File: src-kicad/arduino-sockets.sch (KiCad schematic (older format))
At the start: 48 parts, among them J10 1x8_female_pin_Header_2.54mm, J11 1x6_female_pin_Header_2.54mm, J12 1x6_male_pin_Header_2.54mm, J13 1x6_male_pin_Header_2.54mm, J14 1x6_male_pin_Header_2.54mm, J19 2x4_male_pin_Header_2.54mm, J2 1x6_male_pin_Header_2.54mm, J3 1x6_male_pin_Header_2.54mm, J4 1x10_female_pin_Header_2.54mm, J5 1x8_female_pin_Header_2.54mm, J6 1x6_male_pin_Header_2.54mm, J7 1x8_male_pin_Header_2.54mm, J8 1x8_male_pin_Header_2.54mm, J9 1x8_male_pin_Header_2.54mm, U6 TXB0106, U8 TXB0108, U9 TXB0108

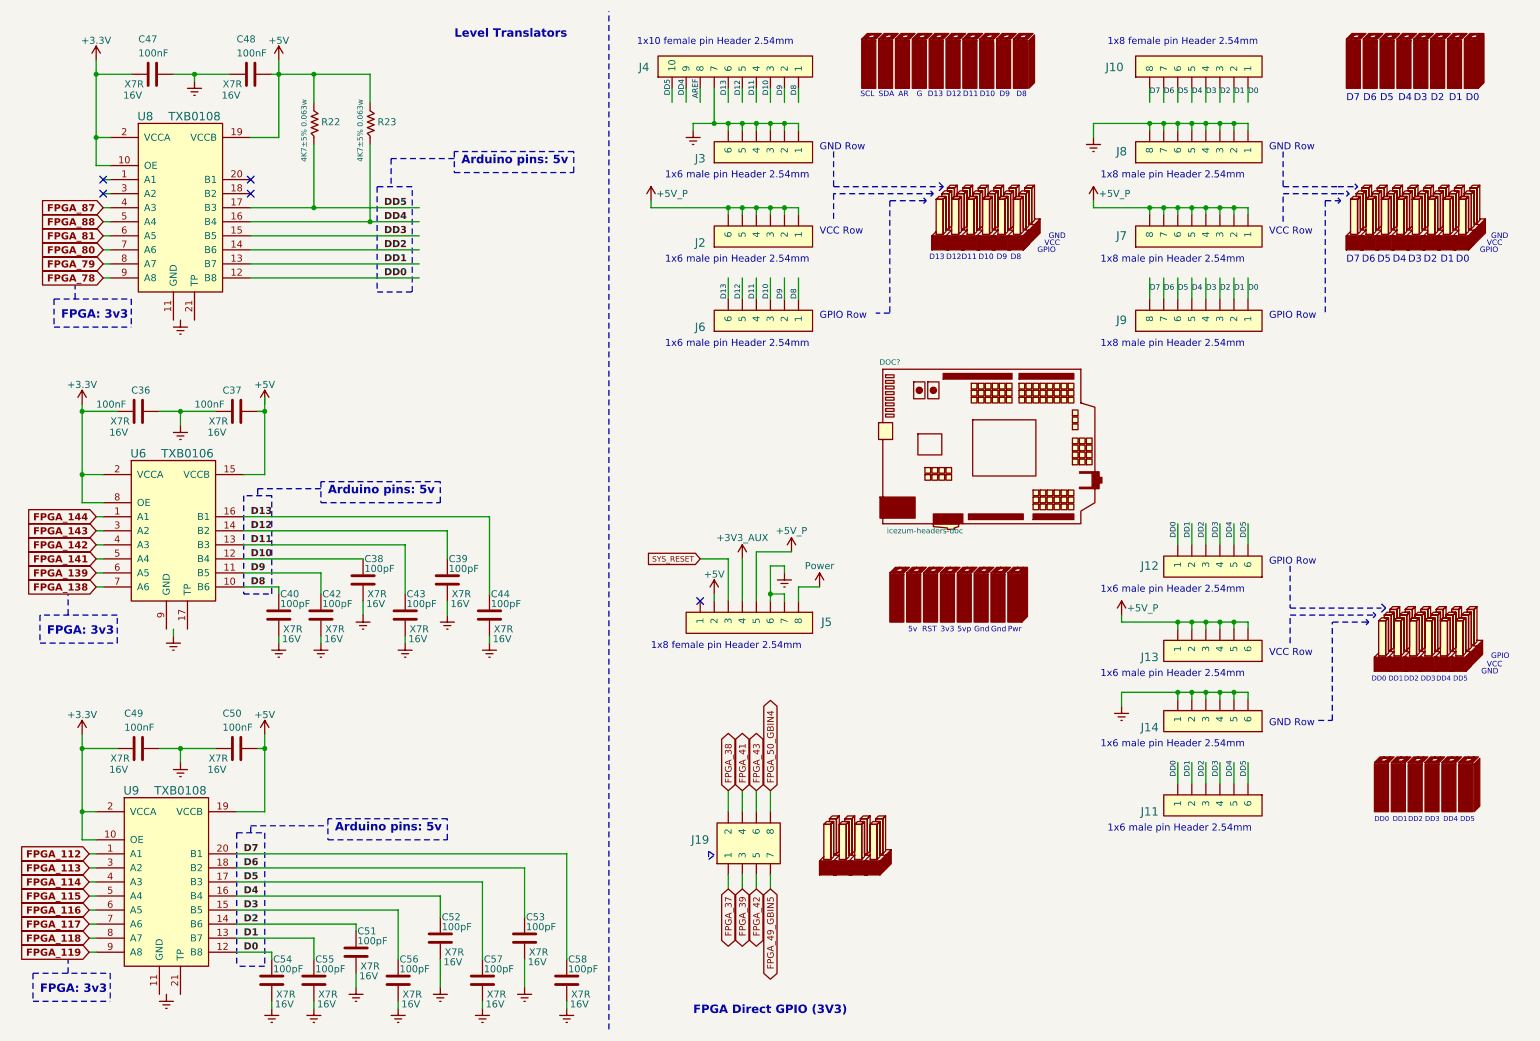
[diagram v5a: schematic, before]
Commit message: Kicad migration: arduino-sockets.sch finished
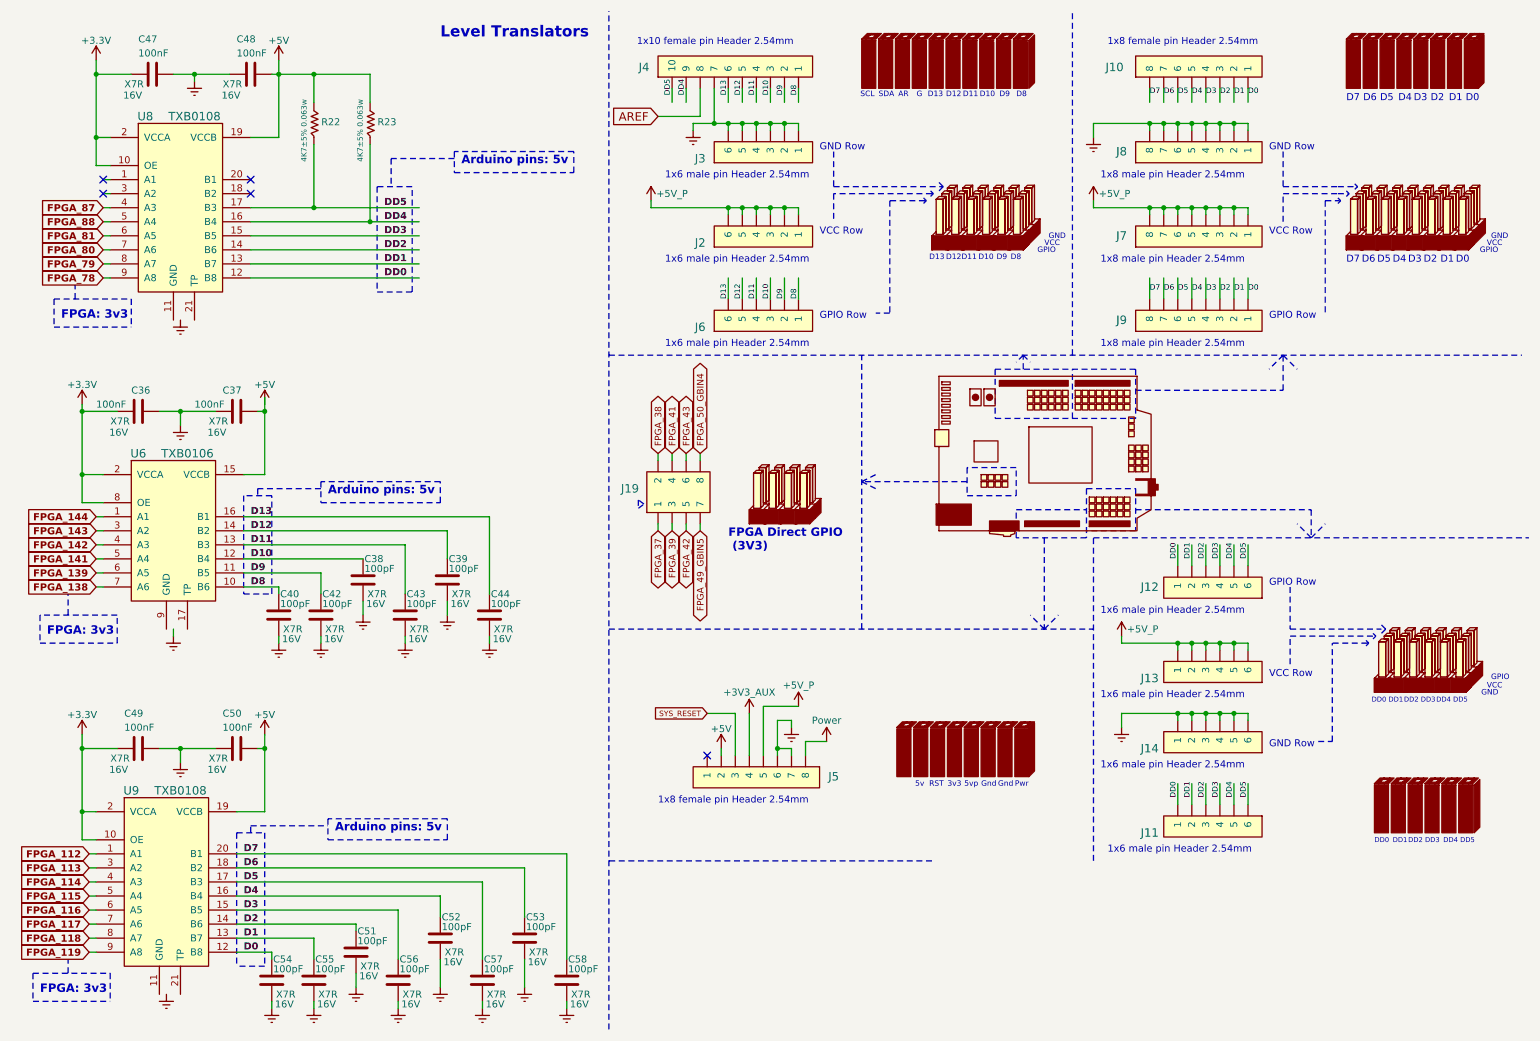
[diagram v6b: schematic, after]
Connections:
- wire segments 218 -> 219
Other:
- note added: "FPGA Direct GPIO\n (3V3)"
- note removed: "FPGA Direct GPIO (3V3)"
- moved on the sheet: J11, J12, J13, J14, J19, J5

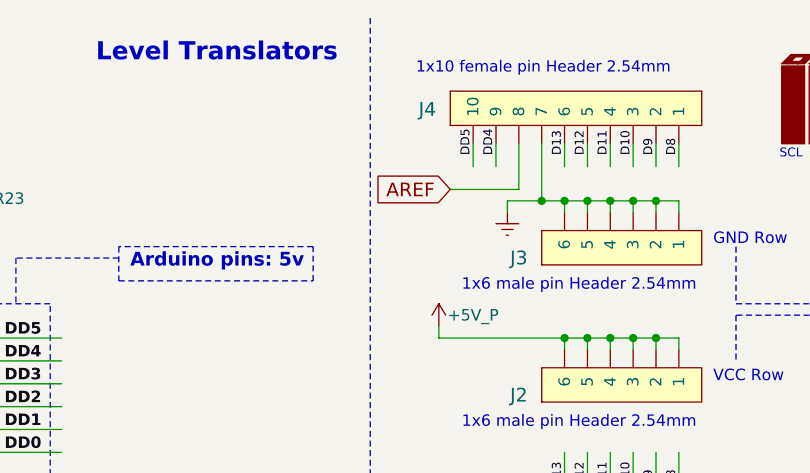
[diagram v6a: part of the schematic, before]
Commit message: Kicad migration: user peripherals added to schematic
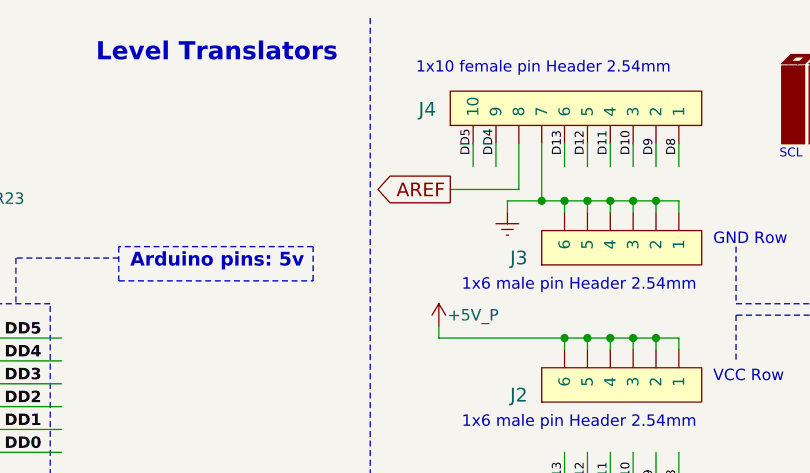
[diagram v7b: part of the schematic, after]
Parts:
- gave numbers to parts that had none: 5
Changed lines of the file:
@@
 LIBS:[4]_Power_Supply-cache
 LIBS:[4]_Power_Supply-rescue
+LIBS:[3]_Connectors_&_IO-cache
 LIBS:icezum-cache
 EELAYER 25 0
@@
 $Descr A4 11693 8268
 encoding utf-8
-Sheet 3 4
+Sheet 3 5
 Title "Arduino sockets & replicating headers"
 Date ""
@@
 	8350 5000 9250 5000
 $Comp
-L +5V_P #PWR?
+L +5V_P #PWR056
 U 1 1 5749A38E
 P 8350 4950
-F 0 "#PWR?" H 8350 4800 50  0001 C CNN
+F 0 "#PWR056" H 8350 4800 50  0001 C CNN
 F 1 "+5V_P" H 8500 5000 50  0000 C CNN
 F 2 "" H 8350 4950 60  0000 C CNN
@@
 Connection ~ 8750 5500
 $Comp
-L GNDREF #PWR?
+L GNDREF #PWR057
 U 1 1 5749D92C
 P 8350 5600
-F 0 "#PWR?" H 8350 5350 50  0001 C CNN
+F 0 "#PWR057" H 8350 5350 50  0001 C CNN
 F 1 "GNDREF" H 8350 5450 50  0001 C CNN
 F 2 "" H 8350 5600 50  0000 C CNN
@@
 1x6 male pin Header 2.54mm
 $Comp
-L 3x6_pin_male_header_DOC doc?
+L 3x6_pin_male_header_DOC doc7
 U 1 1 5749E956
 P 10150 5350
-F 0 "doc?" H 10580 5250 60  0001 C CNN
+F 0 "doc7" H 10580 5250 60  0001 C CNN
 F 1 "3x6_pin_male_header_DOC" H 10670 5910 60  0001 C CNN
 F 2 "" H 10000 6040 60  0000 C CNN
@@
 DD0
 $Comp
-L 1x6_pin_female_header_DOC doc?
+L 1x6_pin_female_header_DOC doc8
 U 1 1 574A45E5
 P 10150 6350
-F 0 "doc?" H 10600 6280 60  0001 C CNN
+F 0 "doc8" H 10600 6280 60  0001 C CNN
 F 1 "1x6_pin_female_header_DOC" H 10600 6850 60  0001 C CNN
 F 2 "" H 10000 7050 60  0000 C CNN
@@
 NoConn ~ 5400 5800
 $Comp
-L +5V #PWR?
+L +5V #PWR058
 U 1 1 574A6429
 P 5500 5750
-F 0 "#PWR?" H 5500 5600 50  0001 C CNN
+F 0 "#PWR058" H 5500 5600 50  0001 C CNN
 F 1 "+5V" H 5500 5890 50  0000 C CNN
 F 2 "" H 5500 5750 50  0000 C CNN
@@
 SYS_RESET
 $Comp
-L +3V3_AUX #PWR?
+L +3V3_AUX #PWR059
 U 1 1 574A74E7
 P 5700 5500
-F 0 "#PWR?" H 5700 5350 50  0001 C CNN
+F 0 "#PWR059" H 5700 5350 50  0001 C CNN
 F 1 "+3V3_AUX" H 5700 5650 50  0000 C CNN
 F 2 "" H 5700 5500 60  0000 C CNN
@@
 	5700 5800 5700 5500
 $Comp
-L +5V_P #PWR?
+L +5V_P #PWR060
 U 1 1 574A7C93
 P 6050 5450
-F 0 "#PWR?" H 6050 5300 50  0001 C CNN
+F 0 "#PWR060" H 6050 5300 50  0001 C CNN
 F 1 "+5V_P" H 6050 5600 50  0000 C CNN
 F 2 "" H 6050 5450 60  0000 C CNN
@@
 	6000 5550 6000 5600
 $Comp
-L GNDREF #PWR?
+L GNDREF #PWR061
 U 1 1 574A8D14
 P 6000 5600
-F 0 "#PWR?" H 6000 5350 50  0001 C CNN
+F 0 "#PWR061" H 6000 5350 50  0001 C CNN
 F 1 "GNDREF" H 6000 5450 50  0001 C CNN
 F 2 "" H 6000 5600 50  0000 C CNN
@@
 Connection ~ 5900 5750
 $Comp
-L Power #PWR?
+L Power #PWR062
 U 1 1 574A903A
 P 6250 5700
-F 0 "#PWR?" H 6250 5550 50  0001 C CNN
+F 0 "#PWR062" H 6250 5550 50  0001 C CNN
 F 1 "Power" H 6250 5850 50  0000 C CNN
 F 2 "" H 6250 5700 60  0000 C CNN
@@
 	6100 5700 6250 5700
 $Comp
-L 1x8_pin_female_header_DOC doc?
+L 1x8_pin_female_header_DOC doc6
 U 1 1 574A9732
 P 6750 5950
-F 0 "doc?" H 7200 5880 60  0001 C CNN
+F 0 "doc6" H 7200 5880 60  0001 C CNN
 F 1 "1x8_pin_female_header_DOC" H 7200 6450 60  0001 C CNN
 F 2 "" H 6600 6650 60  0000 C CNN
@@
 	4950 4010 4910 3980
 $Comp
-L 2x4_pin_male_header_DOC doc?
+L 2x4_pin_male_header_DOC doc5
 U 1 1 574B214C
 P 5700 4150
-F 0 "doc?" H 5950 4060 60  0001 C CNN
+F 0 "doc5" H 5950 4060 60  0001 C CNN
 F 1 "2x4_pin_male_header_DOC" H 5970 4650 60  0001 C CNN
 F 2 "" H 5550 4840 60  0000 C CNN
@@
 $EndComp
 $Comp
-L icezum-headers-doc DOC?
+L icezum-headers-doc DOC1
 U 1 1 574B39A3
 P 7050 4200
-F 0 "DOC?" H 7100 5350 39  0001 C CNN
+F 0 "DOC1" H 7100 5350 39  0001 C CNN
 F 1 "icezum-headers-doc" H 7350 4150 39  0001 C CNN
 F 2 "" H 7290 4690 39  0000 C CNN
@@
 Wire Notes Line
 	9700 4250 9800 4150
-Text GLabel 5050 1250 0    60   Input ~ 0
+Text GLabel 5050 1250 0    60   Output ~ 0
 AREF
 Wire Wire Line
